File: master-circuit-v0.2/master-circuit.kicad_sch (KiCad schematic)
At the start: 104 parts, among them U6 20nF 5%

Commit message: Convert to kicad 10.
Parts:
- CARD1, D1, D2, D3, D4, D6, D7, D8, D9, H1, H2, I2C1, I2C2, LED1, SCREEN1, SW1, SW2, U1, U10, U11, U17, U18, U19, U3, U4, U5, U8, U9, USB1, USB2: value ~ -> (none)
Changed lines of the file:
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@@
 (kicad_sch
-	(version 20250114)
+	(version 20260306)
 	(generator "eeschema")
-	(generator_version "9.0")
+	(generator_version "10.0")
 	(paper "A2")
 	(title_block

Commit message: Working on new circuit.
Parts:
- removed C15, C25, C26, C33: 100nF, Library:C0603, symbol Library:CC0603KRX7R9BB104 Capacitor 100nF
- removed C27, C28: 330pF, Library:C0603, symbol Library:CL10C331JB8NNNC Capacitor 330pF
- removed D1, D9: (no value), Library:SOD-123_L2.7-W1.6-LS3.7-RD-1, symbol Library:B5819W_C8598 Schottky diode
- removed D2: (no value), Library:SOT-23-3_L3.0-W1.7-P0.95-LS2.9-BR, symbol Library:PSM712-LF-T7 ETV/ESD Diodes
- removed R13, R28: 10kΩ, Library:R0603, symbol Library:0603WAF1002T5E Resistor 10kΩ
- removed R19, R20, R38: 5mΩ, Library:R2512 Shunt with Kelvin connections, symbol Library:RLP25FEGMR005 Shunt resistor 5mΩ 1%
- removed U8: (no value), Library:DHVQFN-16_L3.5-W2.5-P0.50-BL-EP, symbol Library:RS595SXTQW16 Shift Register
- removed U9: (no value), Library:QFN-14_L2.5-W2.5-P0.50-TL-EP1.4, symbol Library:HUSB311BLA USB dual role PD
- removed USB1: (no value), Library:USB-C-SMD_TYPE-C16PIN, symbol Library:TYPE-C16PIN USB connector
- added C25, C59, C63, C65, C71, C84, C85: 1uF, Library:C0603, symbol Library:CL10A105KB8NNNC Capacitor 1uF
- added C38, C39, C42, C43, C44, C45, C60, C61, C62, C66, C67, C68, C70: 100nF, Library:C0603, symbol Library:CC0603KRX7R9BB104 Capacitor 100nF
- added C64, C69: 15pF, Library:C0402, symbol Library:0402CG150J500NT Capacitor 15pF
- added D13: (no value), Library:SOD-123_L2.7-W1.6-LS3.7-RD-1, symbol Library:B5819W_C8598 Schottky diode
- added Q10, Q9: (no value), Library:SOT-23-3_L2.9-W1.3-P1.90-LS2.4-BR, symbol Library:SS8050_C2150 NPN BJT transistor
- added R19, R42, R43, R44, R51, R52, R53: 10kΩ, Library:R0603, symbol Library:0603WAF1002T5E Resistor 10kΩ
- added R48: 1mΩ, Library:R2725, symbol Library:YLR25-4-1F-W shunt resistor 1mΩ 1%
- added R50: 12kΩ, Library:R0603, symbol Library:0603WAF1202T5E Resistor 12kΩ
- added U13, U9: (no value), Library:TSSOP-24_L7.8-W4.4-P0.65-LS6.4-BL, symbol Library:TCA9548APWR I2C Multiplexer 8 way
- added U14, U15: (no value), Library:TSSOP-16_L5.0-W4.4-P0.65-LS6.4-BL, symbol Library:PCA9557PW,118 GPIO expander 8 way
- added U16: (no value), Library:TSSOP-20_L6.5-W4.4-P0.65-LS6.4-BL, symbol Library:INA4181A1IPWR Current amplifier
- added U20: (no value), Library:WQFN-16_L3.0-W3.0-P0.50-TL-EP1.7, symbol Library:ADS7128IRTER 8 way ADC with I2C
- added U24: (no value), Library:QFN-64_L9.0-W9.0-P0.50-BL-EP4.8, symbol Library:USB2517-JZX 7-way USB hub
- added U35: (no value), symbol Library:Display_2.8inch_ILI9341
- added X2: 24MHz, Library:CRYSTAL-SMD_4P-L3.2-W2.5-BL, symbol Library:X322524MSB4SI Crystal oscillator 24MHz
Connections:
- net SENSORS_CC1 is gone; now on net CC1: USB2.A5 (CC1)
- net SENSORS_CC2 is gone; now on net CC2: USB2.B5 (CC2)
- net SENSORS_VBUS is gone; now on net VBUS: R40.1
- net SENSORS_VBUS_PINS is gone; now on net VBUS: USB2.A4B9 (VBUS), USB2.B4A9 (VBUS)
- net SENSOR_BOOT0/STOP is gone; now on net BOOT0: USB2.B8 (SBU2)
- net SENSOR_NRST is gone; now on net ENABLE-ESP32: USB2.A8 (SBU1)
- net VBATTERY_PINS is gone; now on net VBATTERY: H2.1, U19.6, U19.7, U19.8
- net 3V3: now also R30.1, C42.2, C43.2, C44.2, C45.2, C59.2, C60.2, C68.2, C84.2, C85.2, R19.2, R42.1, R51.2, U13.1 (A0), U13.2 (A1), U13.21 (A2), U13.24 (VCC), U14.16 (VDD), U15.16 (VDD), U15.3 (A0), U24.24 (VDD33CR), U24.44 (VBUS_DET), U24.46 (VDD33), U35.1 (VCC), U9.24 (VCC); no longer R30.2
- net 3V3A: now also C38.2, C39.2, C61.2, C62.2, C66.2, C67.2, C70.2, C71.2, U16.5 (VS), U24.10 (VDDA33), U24.5 (VDDA33), U24.52 (VDDA33), U24.57 (VDDA33), U24.64 (VDD33PLL)
- net BATTERY_1: now also U15.13 (IO6); no longer U1.10 (IO17)
- net BATTERY_2: now also U15.14 (IO7); no longer U1.25 (IO48)
- net BOOT0: now also C25.2, Q10.3 (C), R42.2
- net GND: now also C25.1, C38.1, C39.1, C42.1, C43.1, C44.1, C45.1, C59.1, C60.1, C61.1, C62.1, C63.1, C64.2, C65.1, C66.1, C67.1, C68.1, C69.1, C70.1, C71.1, C84.1, C85.1, R50.2, R52.1, R53.1, U13.12 (GND), U14.3 (A0), U14.4 (A1), U14.5 (A2), U14.8 (VSS), U15.4 (A1), U15.5 (A2), U15.8 (VSS), U16.16 (GND), U20.17 (EP), U20.9 (GND), U24.65 (EP), U35.2 (GND), U9.1 (A0), U9.12 (GND), U9.2 (A1), U9.21 (A2), X2.2 (GND), X2.4 (GND); no longer USB2.1 (SHELL), USB2.2 (SHELL), USB2.3 (SHELL), USB2.4 (SHELL)
- net I2C1_SCL: now also SCREEN1.6, U18.6 (SDA/SDI/SDO), U14.1 (SCL), U15.1 (SCL), U20.13 (SCL), U9.22 (SCL); no longer I2C1.4
- net I2C1_SDA: now also SCREEN1.5, U18.4 (SCL/SPC), U14.2 (SDA), U15.2 (SDA), U20.14 (SDA), U9.23 (SDA); no longer I2C1.3
- net I2C2_SCL: now also U13.22 (SCL); no longer I2C2.4, SCREEN1.6, U18.6 (SDA/SDI/SDO)
- net I2C2_SDA: now also U13.23 (SDA); no longer I2C2.3, SCREEN1.5, U18.4 (SCL/SPC)
- net REFERENCE: now also U16.1 (REF1), U16.12 (REF3), U16.20 (REF4), U16.9 (REF2), U20.15 (AIN0/GPIO0)
- net VBUS: now also D13.2 (+)
- net VCC: now also C21.2, C22.2, D3.1 (-), U4.3 (VIN), D13.1 (-), R48.2 (Shunt-2)
- net RTS: now reaches U10.24 (RTS)
- net RTS: now also Q9.2 (E), R44.2
- net DTR: now reaches U10.28 (DTR)
- net DTR: now also Q10.2 (E), R43.2
- net +Probe-4: now reaches U11.17 (IN+4)
- net -Probe-4: now reaches U11.18 (IN±4)
- net SERVO4_CURRENT: now reaches U11.19 (OUT4)
- net SERVO4_CURRENT: now also U20.3 (AIN4/GPIO4)
- net BATTERY_CURRENT: no longer names the net of U1.8 (IO15)
- net BATTERY_CURRENT: no longer U11.8 (OUT2)
- net I2C1_BOOT0/STOP: no longer names the net of I2C1.6
- net I2C1_NRST: no longer names the net of I2C1.5
- net I2C2_BOOT0/STOP: no longer names the net of I2C2.6
- net I2C2_NRST: no longer names the net of I2C2.5
- net RESET renamed ENABLE-ESP32
- net ENABLE-ESP32: now also Q9.3 (C)
- net SENSORS_USB_D+ renamed GUEST_USB_D+
- net GUEST_USB_D+: now also U5.4 (D+)
- net SENSORS_USB_D- renamed GUEST_USB_D-
- net GUEST_USB_D-: now also U5.5 (D-)
- net SENSOR_CURRENT renamed NRESET_ALL_MULTIPLEXERS
- net NRESET_ALL_MULTIPLEXERS: now also R29.1, U13.3 (RESET#), U14.15 (RESET#), U15.15 (RESET#), U24.43 (RESET_N), U9.3 (RESET#); no longer U11.13 (OUT3)
- net SHIFT_BANK1_LATCH: no longer names the net of U1.16 (IO46)
- net SHIFT_BANK2_LATCH: no longer names the net of U1.26 (IO45)
- net SHIFT_OE: no longer names the net of U1.24 (IO47)
- net SHIFT_OE: no longer R30.1
- net SPI3_CLK: no longer names the net of U1.23 (IO21)
- net SPI3_CLK: no longer R29.1
- net SPI3_MISO: no longer names the net of U1.22 (IO14)
- net SPI3_MOSI: no longer names the net of U1.17 (IO9)
- net USB_D+ renamed INTERNAL_GUEST_USB_D+
- net INTERNAL_GUEST_USB_D+: no longer U5.4 (D+)
- net USB_D- renamed INTERNAL_GUEST_USB_D-
- net INTERNAL_GUEST_USB_D-: no longer U5.5 (D-)
- net VBUS_CURRENT renamed SERVO1_CURRENT
- net SERVO1_CURRENT: now also U20.16 (AIN1/GPIO1); no longer U1.5 (IO5)
- new net: R51.1, U24.45 (SUSP_IND/LOCAL_PWR/NON_REM0)
- new net: Q10.1 (B), R44.1
- new net: C63.2, U24.25 (VDD18)
- new net: R52.2, U24.40 (SDA/SMBDATA/NON_REM1)
- new net: R50.1, U24.63 (RBIAS)
- new net: Q9.1 (B), R43.1
- new net +Probe-5: U16.4 (IN+1)
- new net +Probe-6: U16.6 (IN+2)
- new net +Probe-7: U16.15 (IN+3)
- new net +Probe-8: R48.4 (Probe-2), U16.17 (IN+4)
- new net -Probe-5: U16.3 (IN±1)
- new net -Probe-6: U16.7 (IN±2)
- new net -Probe-7: U16.14 (IN±3)
- new net -Probe-8: R48.3 (Probe-1), U16.18 (IN±4)
- new net CFG_SEL0: R53.2, U24.41 (SCL/SMBCLK/CFG_SEL0)
- new net CFG_SEL1: R19.1, U24.42 (HS_IND/CFG_SEL1)
- new net CFG_SEL2: R30.2, U24.13 (CFG_SEL2)
- new net I2C_EXTERNAL1_SCL: I2C1.4, U13.18 (SC6)
- new net I2C_EXTERNAL1_SDA: I2C1.3, U13.17 (SD6)
- new net I2C_EXTERNAL2_SCL: I2C2.4, U13.20 (SC7)
- new net I2C_EXTERNAL2_SDA: I2C2.3, U13.19 (SD7)
- new net PRTPWR1: U24.29 (PRTPWR1)
- new net PRTPWR2: U24.26 (PRTPWR2)
- new net PRTPWR3: U24.23 (PRTPWR3)
- new net PRTPWR4: U24.20 (PRTPWR4)
- new net PRTPWR5: U24.30 (PRTPWR5)
- new net PRTPWR6: U24.39 (PRTPWR6)
- new net PRTPWR7: U24.36 (PRTPWR7)
- new net SERVO1_BOOT0: U14.6 (IO0), U9.4 (SD0), U9.7 (SC1)
- new net SERVO1_NRST: U14.7 (IO1), U9.5 (SC0), U9.6 (SD1)
- new net SERVO2_BOOT0: U14.9 (IO2), U9.11 (SC3), U9.8 (SD2)
- new net SERVO2_CURRENT: U11.8 (OUT2), U20.1 (AIN2/GPIO2)
- new net SERVO2_NRST: U14.10 (IO3), U9.10 (SD3), U9.9 (SC2)
- new net SERVO3_BOOT0: U14.11 (IO4), U9.13 (SD4), U9.16 (SC5)
- new net SERVO3_CURRENT: U11.13 (OUT3), U20.2 (AIN3/GPIO3)
- new net SERVO3_NRST: U14.12 (IO5), U9.14 (SC4), U9.15 (SD5)
- new net SERVO4_BOOT0: U14.13 (IO6), U9.17 (SD6), U9.20 (SC7)
- new net SERVO4_NRST: U14.14 (IO7), U9.18 (SC6), U9.19 (SD7)
- new net SERVO5_BOOT0: U13.4 (SD0), U13.7 (SC1), U15.6 (IO0)
- new net SERVO5_CURRENT: U16.2 (OUT1), U20.4 (AIN5/GPIO5)
- new net SERVO5_NRST: U13.5 (SC0), U13.6 (SD1), U15.7 (IO1)
- new net SERVO6_BOOT0: U13.11 (SC3), U13.8 (SD2), U15.9 (IO2)
- new net SERVO6_CURRENT: U16.8 (OUT2), U20.5 (AIN6/GPIO6)
- new net SERVO6_NRST: U13.10 (SD3), U13.9 (SC2), U15.10 (IO3)
- new net SERVO7_BOOT0: U13.13 (SD4), U13.16 (SC5), U15.11 (IO4)
- new net SERVO7_CURRENT: U16.13 (OUT3), U20.6 (AIN7/GPIO7)
- new net SERVO7_NRST: U13.14 (SC4), U13.15 (SD5), U15.12 (IO5)
- new net TOUCH_CS: U1.10 (IO17)
- new net USBDN1_D+: U24.2 (USBDN1_DP/PRT_DIS_P1)
- new net USBDN1_D-: U24.1 (USBDN1_DM/PRT_DIS_M1)
- new net USBDN2_D+: U24.4 (USBDN2_DP/PRT_DIS_P2)
- new net USBDN2_D-: U24.3 (USBDN2_DM/PRT_DIS_M2)
- new net USBDN3_D+: U24.7 (USBDN3_DP/PRT_DIS_P3)
- new net USBDN3_D-: U24.6 (USBDN3_DM/PRT_DIS_M3)
- new net USBDN4_D+: U24.9 (USBDN4_DP/PRT_DIS_P4)
- new net USBDN4_D-: U24.8 (USBDN4_DM/PRT_DIS_M4)
- new net USBDN5_D+: U24.12 (USBDN5_DP/PRT_DIS_P5)
- new net USBDN5_D-: U24.11 (USBDN5_DM/PRT_DIS_M5)
- new net USBDN6_D+: U24.54 (USBDN6_DP/PRT_DIS_P6)
- new net USBDN6_D-: U24.53 (USBDN6_DM/PRT_DIS_M6)
- new net USBDN7_D+: U24.56 (USBDN7_DP/PRT_DIS_P7)
- new net USBDN7_D-: U24.55 (USBDN7_DM/PRT_DIS_M7)
- new net VCC_CURRENT: U1.5 (IO5), U16.19 (OUT4)
- new net VCC_PROBE: R48.1 (Shunt-1)
- new net VDD18PLL: C65.2, U24.62 (VDD18PLL)
- new net XTAL1: C64.1, U24.61 (XTAL1/CLKIN), X2.1 (OSC1)
- new net XTAL2: C69.2, U24.60 (XTAL2), X2.3 (OSC2)
- new net nOCS1: U24.28 (OCS1_N)
- new net nOCS2: U24.27 (OCS2_N)
- new net nOCS3: U24.22 (OCS3_N)
- new net nOCS4: U24.21 (OCS4_N)
- new net nOCS5: U24.35 (OCS5_N)
- new net nOCS6: U24.38 (OCS6_N)
- new net nOCS7: U24.37 (OCS7_N)
- no-connect marks 52 -> 60
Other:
- removed sheet back-to-back-mosfets3
- removed sheet group-of-8-servo-connectors
- removed sheet group-of-8-servo-connectors1
- removed sheet group-of-8-servo-connectors2
- added sheet servo-usb-connector (servo-usb-connector.kicad_sch)
- added sheet servo-usb-connector1 (servo-usb-connector.kicad_sch)
- added sheet servo-usb-connector2 (servo-usb-connector.kicad_sch)
- added sheet servo-usb-connector3 (servo-usb-connector.kicad_sch)
- added sheet servo-usb-connector4 (servo-usb-connector.kicad_sch)
- added sheet servo-usb-connector5 (servo-usb-connector.kicad_sch)
- added sheet servo-usb-connector6 (servo-usb-connector.kicad_sch)
- note added: "5V and 3V3 power regulator and filtering"
- note added: "Battery and CAN bus to interface with external motors."
- note added: "Battery with 2 GPIO to interface with tool batteries."
- note added: "Do i wanna do the debug lines?"
- note added: "Double up mosfets to battery connector. The ones we chose here are rated to 40A continnous, but we are close to being limited by copper trace width."
- note added: "Eusebiu - USB C - guest for programming"
- note added: "Guard the external I2C lines behind the multiplexer connected to the 2nd ESP32 I2C. This way only the multiplexer address is a potential conflict on the bus (in this case 1110111) while the internal chips are on the 1st I2C line of the ESP32."
- note added: "Main power comes from the VCC bus, but we have diodes to wakeup the microcontroller, which turns on the VCC line."
- note added: "Power connection switch between battery or 20V USB-C"
- note added: "Probably need a small transistor to turn on screen (needs 3.3V)."
- note added: "See: https://dl.espressif.com/dl/schematics/SCH_ESP32-S3-DevKitC-1_V1.1_20220413.pdf"
- note added: "Strapping pin: pull-up too weak, need our own"
- note added: "UART pads for debugging."
- note added: "needs to be 90ohm impedance?"
- note removed: "3V3 power regulator and filtering"
- note removed: "Eusebiu - USB C - The guest"
- note removed: "Eusebiu - USB C - The host"
- note removed: "Ground the shell for an upstream device."
- note removed: "I2C connectors and battery level LEDs"
- note removed: "Note: pullups included in ESP32-S3 series."
- note removed: "Plugin connectors: UART, Battery, and Power + CAN Bus"
- note removed: "Power connection switch between battery or 20V USB-C or both (to charge)."
- note removed: "SBU1 and SBU2 are coonected to Reset and Boot0 pins so we are consistent with the mini drive."
- note removed: "Strapping pin: pull-up"
- note removed: "USB Source/Sink Controller"
- moved on the sheet: C12, C13, C14, C16, C17, C18, C20, C21, C22, C23, C24, C30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
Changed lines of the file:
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@@
 	(title_block
 		(title "Hex master motor control circuit")
+		(date "2026-06-05")
+		(rev "version 0.2")
 		(company "Hex Robotics Limited")
 		(comment 1 "Author: Calin Mocanu")

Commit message: Almost complete new master circuit schematic.
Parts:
- removed C14: 100nF, Library:C0603, symbol Library:CC0603KRX7R9BB104 Capacitor 100nF
- removed CARD1: (no value), Library:TF-SMD_TF-01A, symbol Library:TF-01A TF Card reader
- removed R19, R53: 10kΩ, Library:R0603, symbol Library:0603WAF1002T5E Resistor 10kΩ
- removed R48: 1mΩ, Library:R2725, symbol Library:YLR25-4-1F-W shunt resistor 1mΩ 1%
- removed SCREEN1: (no value), Library:FPC-SMD_18P-P0.50_FPC-05F-18PH20, symbol Library:FPC-05F-18PH20 Connector 18P 0.5mm spacing FPC
- removed U20: (no value), Library:WQFN-16_L3.0-W3.0-P0.50-TL-EP1.7, symbol Library:ADS7128IRTER 8 way ADC with I2C
- added R34: 1mΩ, Library:R2725 Shunt with Kelvin connections, symbol Library:YLR25-4-1F-W shunt resistor 1mΩ 1%
- U35: footprint (none) -> Library:MSP2807 OLED with touchescreen and SD card; now left out of the parts list
- renumbered USB2 to USB0
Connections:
- net BATTERY_1 is gone; now on net GPIO1: H2.2, U15.13 (IO6)
- net BATTERY_2 is gone; now on net GPIO2: H2.3, U15.14 (IO7)
- net CFG_SEL0 is gone; now on net I2C1_SCL: U24.41 (SCL/SMBCLK/CFG_SEL0)
- net +Probe-8: now also R34.4 (Probe-2)
- net -Probe-8: now also R34.3 (Probe-1)
- net 3V3: no longer R11.2, R12.2, R30.1
- net CAN_RX: now also U1.22 (IO14); no longer U1.38 (IO2)
- net CAN_TX: now also U1.23 (IO21); no longer U1.39 (IO1)
- net CFG_SEL1: now also R52.2
- net CONNECT_BATTERY: now also R11.2, U1.26 (IO45); no longer U1.7 (IO7)
- net CONNECT_VBUS: now also R12.2, U1.16 (IO46); no longer U1.6 (IO6)
- net FSPICLK/SPI2_CLK: now also D4.2 (A1), U35.10 (T_CLK), U35.18 (SD_SCK), U35.7 (SCK); no longer D6.1 (A1)
- net FSPICS0/MEMORY_CS: now also D6.1 (A1), U35.15 (SD_CS); no longer D4.1 (A1)
- net FSPID/SPI2_MOSI: now also U35.12 (T_DIN), U35.16 (SD_MOSI), U35.6 (SDI/MOSI)
- net FSPIQ/SPI2_MISO: now also D4.1 (A1), U35.13 (T_DO), U35.17 (SD_MISO), U35.9 (SD0/MISO); no longer D4.2 (A1)
- net GND: now also R11.1, R12.1, R30.1
- net I2C1_SDA: now also U24.40 (SDA/SMBDATA/NON_REM1)
- net INTERNAL_GUEST_USB_D+: now also U24.59 (USBUP_DP)
- net INTERNAL_GUEST_USB_D-: now also U24.58 (USBUP_DM)
- net NRESET_ALL_MULTIPLEXERS: now also U1.24 (IO47); no longer U1.12 (IO8)
- net REFERENCE: now also U1.17 (IO9); no longer U1.15 (IO3)
- net SCREEN_CS: now also U35.3 (CS)
- net SCREEN_DC: now also U35.5 (DC)
- net SCREEN_LED: now also U1.25 (IO48), U35.8 (LED)
- net SCREEN_RESET: now also U35.4 (RESET)
- net SERVO1_CURRENT: now also U1.39 (IO1)
- net SERVO2_CURRENT: now also U1.38 (IO2)
- net SERVO3_CURRENT: now also U1.15 (IO3)
- net SERVO4_CURRENT: now also U1.4 (IO4)
- net SERVO5_CURRENT: now also U1.5 (IO5)
- net SERVO6_CURRENT: now also U1.6 (IO6)
- net SERVO7_CURRENT: now also U1.7 (IO7)
- net TOUCH_CS: now also U35.11 (T_CS)
- net TOUCH_INT: now also U35.14 (T_IRQ)
- net VBUS_VOLTAGE: now also U1.8 (IO15); no longer U1.4 (IO4)
- net VCC: now also R34.2 (Shunt-2)
- net VCC_CURRENT: now also U1.12 (IO8); no longer U1.5 (IO5)
- net VCC_PROBE: now also R34.1 (Shunt-1)
- net GPIO1: now reaches I2C1.5
- net GPIO1: now also I2C2.5
- net GPIO2: now reaches I2C1.6
- net GPIO2: now also I2C2.6
- no-connect marks 60 -> 57
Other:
- note added: "ESP32-S3-WROOM-1-N16R8 controller"
- note added: "SDA and SCL are pulled-up at the MCU."
- note added: "Screen, touch, and SD memory card connect to SPI2."
- note added: "There's a transistor on the display board."
- note added: "USB Hub and downstream connectors"
- note removed: "Do i wanna do the debug lines?"
- note removed: "Memory card connects to SPI2"
- note removed: "Probably need a small transistor to turn on screen (needs 3.3V)."
- note removed: "Pull-ups on all SPI lines on the main chip."
- note removed: "TOUCH_RESET always high to enable the chip."
- note removed: "Touch screen: https://www.aliexpress.com/item/1005009132201384.html Description Report Item IPS 1.69 inch TFT LCD Round Screen Size: 1.69 inch LCD Type: TFT Outline Dimensions: 30.07*37.43*1.6mm Active Area: 27.97*32.63mm Number of Dots: 240(RGB)*280 Controller: ST7789T3 Touch IC: CST816T PIN NO.: 18P Display Color: 262K Backlight: White LED Polarizer Mode: Transmissive Data Interface: 4-Wire-SPI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"
- note removed: "needs to be 90ohm impedance?"
- moved on the sheet: C1, C10, C11, C12, C13, C16, C17, C18, C19, C2, C20, C21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
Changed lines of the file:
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@@
 	(generator "eeschema")
 	(generator_version "10.0")
-	(paper "A2")
+	(paper "A1")
 	(title_block
 		(title "Hex master motor control circuit")

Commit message: Drop unused features and arrange components on new master circuit board.
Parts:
- removed H1, H2: (no value), Library:HDR-TH_4P-P2.54-V-M, symbol Library:PZ254V-11-04P_C2691448 Connector 4P 2.54mm spacing
- removed I2C1, I2C2: (no value), Library:FPC-SMD_6P-P0.50_XUNPU_FPC-05F-6PH20, symbol Library:FPC-05F-6PH20 Connector 6P 0.5mm spacing FPC
- removed R1, R3, R7, R8: 10kΩ, Library:R0603, symbol Library:0603WAF1002T5E Resistor 10kΩ
- removed R2, R4, R5: 100kΩ, Library:R0603, symbol Library:0603WAF1003T5E Resistor 100kΩ
- removed R6: 13kΩ, Library:R0603, symbol Library:0603WAF1302T5E Resistor 13kΩ
- added R34, R37, R38, R47, R53, R58, R60, R64: 10kΩ, Library:R0603, symbol Library:0603WAF1002T5E Resistor 10kΩ
- added R45, R48, R56: 100kΩ, Library:R0603, symbol Library:0603WAF1003T5E Resistor 100kΩ
- added R62: 13kΩ, Library:R0603, symbol Library:0603WAF1302T5E Resistor 13kΩ
- added R7: 5mΩ, Library:R2512 Shunt with Kelvin connections, symbol Library:RLP25FEGMR005 Shunt resistor 5mΩ 1%
- renumbered R34 to R8
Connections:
- net SERVO7_BOOT0 is gone; now on net SERVO6_BOOT0: U13.13 (SD4), U13.16 (SC5), U15.11 (IO4)
- net SERVO7_NRST is gone; now on net SERVO6_NRST: U13.14 (SC4), U13.15 (SD5), U15.12 (IO5)
- net USBDN7_D+ is gone; now on net GND: U24.56 (USBDN7_DP/PRT_DIS_P7)
- net USBDN7_D- is gone; now on net GND: U24.55 (USBDN7_DM/PRT_DIS_M7)
- net nOCS7 is gone; now on net 3V3: U24.37 (OCS7_N)
- net +Probe-7: now also R7.4 (Probe-2)
- net -Probe-7: now also R7.3 (Probe-1)
- net 3V3: now also U9.1 (A0), U9.2 (A1), U9.21 (A2), R34.2, R37.2, R53.2, R58.2, R60.2, R64.2; no longer U15.3 (A0)
- net BATTERY_VOLTAGE: now also R38.2, R48.1
- net Buck-FB: now also R56.1, R62.2
- net Buck-Probe-Point: now also R56.2
- net ENABLE-ESP32: now also R37.1
- net FSPID/SPI2_MOSI: now also R34.1
- net GND: now also U15.3 (A0), R38.1, R47.1, R62.1; no longer U9.1 (A0), U9.2 (A1), U9.21 (A2)
- net I2C1_SCL: no longer U14.1 (SCL), U15.1 (SCL), U18.6 (SDA/SDI/SDO), U24.41 (SCL/SMBCLK/CFG_SEL0)
- net I2C1_SDA: no longer U14.2 (SDA), U15.2 (SDA), U18.4 (SCL/SPC), U24.40 (SDA/SMBDATA/NON_REM1)
- net SERVO4_BOOT0: now also U13.4 (SD0), U13.7 (SC1), U15.6 (IO0); no longer U14.13 (IO6), U9.17 (SD6), U9.20 (SC7)
- net SERVO4_NRST: now also U13.5 (SC0), U13.6 (SD1), U15.7 (IO1); no longer U14.14 (IO7), U9.18 (SC6), U9.19 (SD7)
- net SERVO5_BOOT0: now also U13.11 (SC3), U13.8 (SD2), U15.9 (IO2); no longer U13.4 (SD0), U13.7 (SC1), U15.6 (IO0)
- net SERVO5_NRST: now also U13.10 (SD3), U13.9 (SC2), U15.10 (IO3); no longer U13.5 (SC0), U13.6 (SD1), U15.7 (IO1)
- net SERVO6_BOOT0: no longer U13.11 (SC3), U13.8 (SD2), U15.9 (IO2)
- net SERVO6_NRST: no longer U13.10 (SD3), U13.9 (SC2), U15.10 (IO3)
- net VBATTERY: now also R48.2
- net VBUS: now also R45.2
- net VBUS_VOLTAGE: now also R45.1, R47.2
- net VCC: now also R7.2 (Shunt-2)
- net RBIAS: now reaches R50.1, U24.63 (RBIAS)
- net GPIO1: no longer names the net of U15.13 (IO6)
- net GPIO2: no longer names the net of U15.14 (IO7)
- net I2C_EXTERNAL1_SCL: no longer names the net of U13.18 (SC6)
- net I2C_EXTERNAL1_SDA: no longer names the net of U13.17 (SD6)
- net I2C_EXTERNAL2_SCL renamed I2C2_INTERNAL_SDA
- net I2C2_INTERNAL_SDA: now also U15.2 (SDA), U18.4 (SCL/SPC), R64.1
- net I2C_EXTERNAL2_SDA renamed I2C2_INTERNAL_SCL
- net I2C2_INTERNAL_SCL: now also U15.1 (SCL), U18.6 (SDA/SDI/SDO), R60.1
- net PRTPWR7: no longer names the net of U24.36 (PRTPWR7)
- net VCC_PROBE renamed VBATTERY_PROBE
- new net I2C1_INTERNAL_SCL: R53.1, U14.1 (SCL), U24.40 (SDA/SMBDATA/NON_REM1), U9.19 (SD7)
- new net I2C1_INTERNAL_SDA: R58.1, U14.2 (SDA), U24.41 (SCL/SMBCLK/CFG_SEL0), U9.20 (SC7)
- new net VBUS_PROBE: R7.1 (Shunt-1)
- no-connect marks 57 -> 62
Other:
- removed sheet servo-usb-connector6
- note added: "Accelerometer connects to I2C 2 internally after a multiplexer."
- note added: "I2C pull-ups on GPIO multiplexers."
- note added: "Unused port 7"
- note removed: "Accelerometer connects to I2C 2."
- note removed: "Battery with 2 GPIO to interface with tool batteries."
- note removed: "SDA A FPC connector"
- note removed: "SDA B FPC connector"
- note removed: "SDA and SCL are pulled-up at the MCU."
- note removed: "UART pads for debugging."
- moved on the sheet: C44, C45, U15

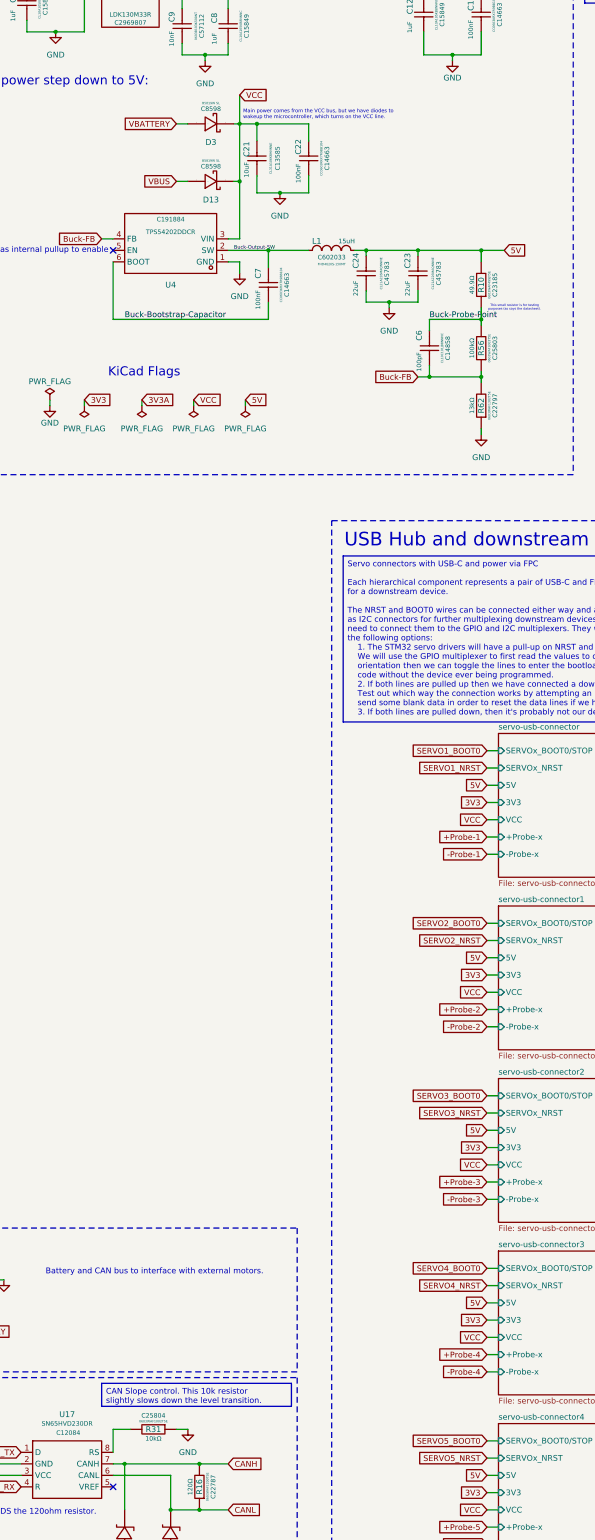
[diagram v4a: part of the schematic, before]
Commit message: Connect one of the USB outputs, outline part placement.
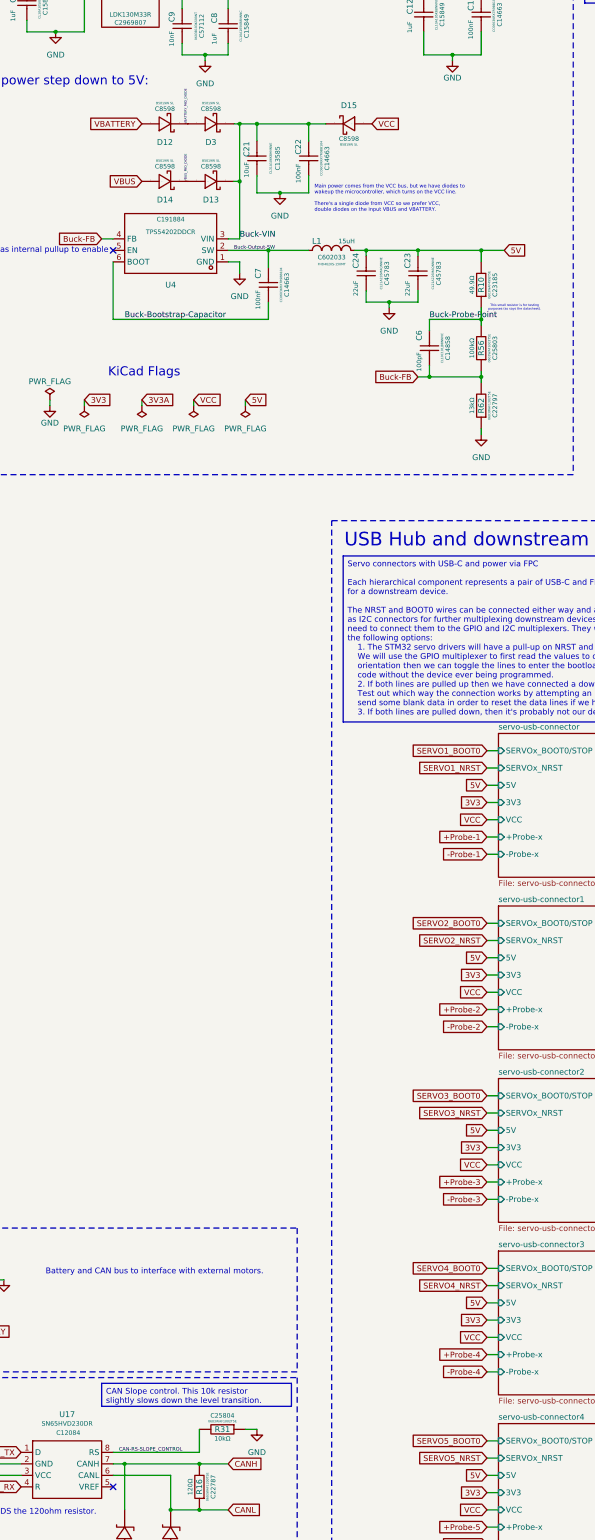
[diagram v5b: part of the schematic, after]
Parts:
- added D12, D14, D15: (no value), Library:SOD-123_L2.7-W1.6-LS3.7-RD-1, symbol Library:B5819W_C8598 Schottky diode
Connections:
- net VBATTERY: now also D12.2 (+); no longer D3.2 (+)
- net VBUS: now also D14.2 (+); no longer D13.2 (+)
- net VCC: now also D15.2 (+); no longer C21.2, C22.2, D13.1 (-), D3.1 (-), U4.3 (VIN)
- net CAN-RS-SLOPE_CONTROL: now reaches R31.2, U17.8 (RS)
- new net Buck-VIN: C21.2, C22.2, D13.1 (-), D15.1 (-), D3.1 (-), U4.3 (VIN)
- new net VBATTERY_MID_DIODE: D12.1 (-), D3.2 (+)
- new net VBUS_MID_DIODE: D13.2 (+), D14.1 (-)
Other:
- note added: "Main power comes from the VCC bus, but we have diodes to wakeup the microcontroller, which turns on the VCC line. There's a single diode from VCC so we prefer VCC, double diodes on the input VBUS and VBATTERY."
- note removed: "Main power comes from the VCC bus, but we have diodes to wakeup the microcontroller, which turns on the VCC line."
- moved on the sheet: R31
